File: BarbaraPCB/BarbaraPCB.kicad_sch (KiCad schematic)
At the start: 138 parts, among them J1 Conn_01x05_Pin, J2 Conn_01x05_Pin, J3 Conn_01x05_Pin_reversed, J4 Conn_01x05_Pin_reversed, SW1 SW_Push, SW10 SW_Push, SW11 SW_Push, SW12 SW_Push, SW13 SW_Push, SW14 SW_Push, SW15 SW_Push, SW16 SW_Push, SW17 SW_Push, SW18 SW_Push, SW19 SW_Push, SW2 SW_Push, SW20 SW_Push, SW21 SW_Push_1.5u, SW22 SW_Push, SW23 SW_Push, SW24 SW_Push, SW25 SW_Push, SW26 SW_Push, SW27 SW_Push, SW28 SW_Push, SW29 SW_Push_1.5u, SW3 SW_Push, SW30 SW_Push, SW31 SW_Push, SW32 SW_Push, SW33 SW_Push, SW34 SW_Push, SW35 SW_Push_1.25u, SW36 SW_Push_1.75u, SW37 SW_Push_1.75u, SW38 SW_Push_1.25u, SW39 SW_Push, SW4 SW_Push, SW40 SW_Push, SW41 SW_Push, SW42 SW_Push, SW43 SW_Push, SW44 SW_Push, SW45 SW_Push_1.5u, SW46 SW_Push_1.5u, SW47 SW_Push_1.5u, SW48 SW_Push_1.5u, SW49 SW_Push, SW5 SW_Push, SW50 SW_Push, SW51 SW_Push, SW52 SW_Push, SW53 SW_Push, SW54 SW_Push_1.25u, SW55 SW_Push_1.75u, SW56 SW_Push_1.75u, SW57 SW_Push_1.25u, SW58 SW_Push, SW59 SW_Push, SW6 SW_Push, SW60 SW_Push, SW61 SW_Push, SW62 SW_Push, SW63 SW_Push, SW64 SW_Push_1.5u, SW65 SW_Push_1.5u, SW66 SW_Push_1.5u, SW67 SW_Push_1.5u, SW7 SW_Push, SW8 SW_Push, SW9 SW_Push

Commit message: Soundbauteile hinzugefügt
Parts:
- added BZ1: Buzzer, Buzzer_Beeper:MagneticBuzzer_StarMicronics_QMB-105, symbol Device:Buzzer
- added C1: 100n, Capacitor_THT:C_Disc_D5.0mm_W2.5mm_P5.00mm, symbol Device:C
- added C2: 100n, Capacitor_SMD:C_0805_2012Metric_Pad1.18x1.45mm_HandSolder, symbol Device:C
- added D48: 1N4148, TFL:Diode-dual, symbol Diode:1N4148
- added J5: Connector for PAM8403 Amp, Connector_PinHeader_2.54mm:PinHeader_1x04_P2.54mm_Vertical, symbol Connector:Conn_01x04_Socket
- added Q2: PN2222A, Package_TO_SOT_THT:TO-92_Inline, symbol Transistor_BJT:PN2222A
- added R1, R2: 1K, TFL:Diode-dual, symbol Device:R
- added U1: RP2040-Matrix, TFL:RP2040-Gemini-BigHole, symbol PCM_marbastlib-promicroish:RP2040-Matrix
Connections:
- net row0: now also U1.4 (P29)
- new net: C1.1, C2.1, J5.4 (Pin_4), R2.2
- new net: R2.1, U1.19 (P13)
- new net: R1.1, U1.9 (P14)
- new net: BZ1.2 (-), D48.2 (A), Q2.3 (C)
- new net: Q2.2 (B), R1.2
- new net +5V: BZ1.1 (+), D48.1 (K), J5.1 (Pin_1), U1.1 (5V)
- new net GND: C1.2, C2.2, J5.2 (Pin_2), J5.3 (Pin_3), Q2.1 (E), U1.2 (GND)
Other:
- note added: "Audio GND"
- note added: "Only add one C, one is SMD, the other THT"

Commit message: Silk und diverse Kleinigkeiten. Productionready?!
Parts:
- R1, R2: footprint TFL:Diode-dual -> TFL:Resistor-dual
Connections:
- net col0: now also U1.21 (P11)
- net col1: now also U1.17 (P7)
- net col2: now also U1.16 (P6)
- net col3: now also U1.15 (P5)
- net col4: now also U1.14 (P4)
- net row0: now also U1.13 (P3); no longer U1.4 (P29)
- net row1: now also U1.22 (P10)
- net row2: now also U1.19 (P13)
- net row3: now also U1.20 (P12)
- net row4: now also U1.9 (P14)
- net row5: now also U1.8 (P15)
- net row6: now also U1.7 (P26)
- net row7: now also U1.6 (P27)
- net row8: now also U1.5 (P28)
- net row9: now also U1.4 (P29)
- net at U1.18 (P8): now also R1.1
- net at R2.1: now also U1.23 (P9); no longer U1.19 (P13)
- no-connect marks 0 -> 1
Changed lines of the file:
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@@
 		(color 0 0 0 0)
 	)
+	(no_connect
+		(at 328.93 59.69)
+	)
 	(wire
 		(pts
@@
 	(wire
 		(pts
-			(xy 311.15 82.55) (xy 311.15 88.9)
-		)
-		(stroke
-			(width 0)
-			(type default)
-		)
-	)
-	(wire
-		(pts
 			(xy 195.58 115.57) (xy 195.58 210.82)
 		)
@@
 	(wire
 		(pts
+			(xy 311.15 82.55) (xy 311.15 88.9)
+		)
+		(stroke
+			(width 0)
+			(type default)
+		)
+	)
+	(wire
+		(pts
 			(xy 154.94 252.73) (xy 128.27 252.73)
 		)
@@
 	(global_label "row8"
 		(shape input)
-		(at 384.81 40.64 90)
+		(at 328.93 64.77 0)
 		(fields_autoplaced yes)
 		(effects
@@
 		)
 		(property "Intersheetrefs" "${INTERSHEET_REFS}"
-			(at 384.81 33.1796 90)
+			(at 336.3904 64.77 0)
 			(hide yes)
 			(show_name no)
@@
 	(global_label "row1"
 		(shape input)
-		(at 267.97 40.64 90)
+		(at 313.69 82.55 270)
 		(fields_autoplaced yes)
 		(effects
@@
 				(size 1.27 1.27)
 			)
-			(justify left)
+			(justify right)
 		)
 		(property "Intersheetrefs" "${INTERSHEET_REFS}"
-			(at 267.97 33.1796 90)
+			(at 313.69 90.0104 90)
 			(hide yes)
 			(show_name no)
@@
 					(size 1.27 1.27)
 				)
-				(justify left)
+				(justify right)
 			)
 		)
@@
 	(global_label "row5"
 		(shape input)
-		(at 334.01 40.64 90)
+		(at 328.93 72.39 0)
 		(fields_autoplaced yes)
 		(effects
@@
 		)
 		(property "Intersheetrefs" "${INTERSHEET_REFS}"
-			(at 334.01 33.1796 90)
+			(at 336.3904 72.39 0)
 			(hide yes)
 			(show_name no)
@@
 	(global_label "row2"
 		(shape input)
-		(at 271.78 40.64 90)
+		(at 321.31 82.55 270)
 		(fields_autoplaced yes)
 		(effects
@@
 				(size 1.27 1.27)
 			)
-			(justify left)
+			(justify right)
 		)
 		(property "Intersheetrefs" "${INTERSHEET_REFS}"
-			(at 271.78 33.1796 90)
+			(at 321.31 90.0104 90)
 			(hide yes)
 			(show_name no)
@@
 					(size 1.27 1.27)
 				)
-				(justify left)
+				(justify right)
 			)
 		)
@@
 	(global_label "row9"
 		(shape input)
-		(at 401.32 40.64 90)
+		(at 328.93 62.23 0)
 		(fields_autoplaced yes)
 		(effects
@@
 		)
 		(property "Intersheetrefs" "${INTERSHEET_REFS}"
-			(at 401.32 33.1796 90)
+			(at 336.3904 62.23 0)
 			(hide yes)
 			(show_name no)
@@
 	(global_label "row3"
 		(shape input)
-		(at 300.99 40.64 90)
+		(at 318.77 82.55 270)
 		(fields_autoplaced yes)
 		(effects
@@
 				(size 1.27 1.27)
 			)
-			(justify left)
+			(justify right)
 		)
 		(property "Intersheetrefs" "${INTERSHEET_REFS}"
-			(at 300.99 33.1796 90)
+			(at 318.77 90.0104 90)
 			(hide yes)
 			(show_name no)
@@
 					(size 1.27 1.27)
 				)
-				(justify left)
+				(justify right)
 			)
 		)
@@
 	(global_label "col0"
 		(shape input)
-		(at 292.1 57.15 180)
+		(at 316.23 82.55 270)
 		(fields_autoplaced yes)
 		(effects
@@
 		)
 		(property "Intersheetrefs" "${INTERSHEET_REFS}"
-			(at 285.0025 57.15 0)
+			(at 316.23 89.6475 90)
 			(hide yes)
 			(show_name no)
@@
 	(global_label "col3"
 		(shape input)
-		(at 278.13 48.26 180)
+		(at 303.53 67.31 180)
 		(fields_autoplaced yes)
 		(effects
@@
 		)
 		(property "Intersheetrefs" "${INTERSHEET_REFS}"
-			(at 271.0325 48.26 0)
+			(at 296.4325 67.31 0)
 			(hide yes)
 			(show_name no)
@@
 	(global_label "col1"
 		(shape input)
-		(at 273.05 49.53 180)
+		(at 303.53 72.39 180)
 		(fields_autoplaced yes)
 		(effects
@@
 		)
 		(property "Intersheetrefs" "${INTERSHEET_REFS}"
-			(at 265.9525 49.53 0)
+			(at 296.4325 72.39 0)
 			(hide yes)
 			(show_name no)
@@
 	(global_label "col2"
 		(shape input)
-		(at 261.62 48.26 180)
+		(at 303.53 69.85 180)
 		(fields_autoplaced yes)
 		(effects
@@
 		)
 		(property "Intersheetrefs" "${INTERSHEET_REFS}"
-			(at 254.5225 48.26 0)
+			(at 296.4325 69.85 0)
 			(hide yes)
 			(show_name no)
@@
 	(global_label "row6"
 		(shape input)
-		(at 350.52 40.64 90)
+		(at 328.93 69.85 0)
 		(fields_autoplaced yes)
 		(effects
@@
 		)
 		(property "Intersheetrefs" "${INTERSHEET_REFS}"
-			(at 350.52 33.1796 90)
+			(at 336.3904 69.85 0)
 			(hide yes)
 			(show_name no)
@@
 	(global_label "col4"
 		(shape input)
-		(at 278.13 52.07 180)
+		(at 303.53 64.77 180)
 		(fields_autoplaced yes)
 		(effects
@@
 		)
 		(property "Intersheetrefs" "${INTERSHEET_REFS}"
-			(at 271.0325 52.07 0)
+			(at 296.4325 64.77 0)
 			(hide yes)
 			(show_name no)
@@
 	(global_label "row4"
 		(shape input)
-		(at 317.5 40.64 90)
+		(at 328.93 74.93 0)
 		(fields_autoplaced yes)
 		(effects
@@
 		)
 		(property "Intersheetrefs" "${INTERSHEET_REFS}"
-			(at 317.5 33.1796 90)
+			(at 336.3904 74.93 0)
 			(hide yes)
 			(show_name no)
@@
 	(global_label "row7"
 		(shape input)
-		(at 367.03 40.64 90)
+		(at 328.93 67.31 0)
 		(fields_autoplaced yes)
 		(effects
@@
 		)
 		(property "Intersheetrefs" "${INTERSHEET_REFS}"
-			(at 367.03 33.1796 90)
+			(at 336.3904 67.31 0)
 			(hide yes)
 			(show_name no)
@@
 		(lib_id "PCM_marbastlib-promicroish:RP2040-Matrix")
 		(at 316.23 68.58 0)
+		(mirror y)
 		(unit 1)
 		(body_style 1)
@@
 		)
 		(property "Datasheet" "https://www.waveshare.com/rp2040-matrix.htm"
-			(at 303.53 54.61 0)
+			(at 328.93 54.61 0)
 			(hide yes)
 			(show_name no)
@@
 			)
 		)
-		(property "Footprint" "TFL:Diode-dual"
+		(property "Footprint" "TFL:Resistor-dual"
 			(at 299.72 73.152 90)
 			(hide yes)
@@
 	(symbol
 		(lib_id "power:+5V")
-		(at 303.53 54.61 90)
+		(at 328.93 54.61 270)
 		(unit 1)
 		(body_style 1)
@@
 		(fields_autoplaced yes)
 		(property "Reference" "#PWR02"
-			(at 307.34 54.61 0)
+			(at 325.12 54.61 0)
 			(hide yes)
 			(show_name no)
@@
 		)
 		(property "Value" "+5V"
-			(at 299.72 54.6099 90)
+			(at 332.74 54.6099 90)
 			(show_name no)
 			(do_not_autoplace no)
@@
 		)
 		(property "Footprint" ""
-			(at 303.53 54.61 0)
+			(at 328.93 54.61 0)
 			(hide yes)
 			(show_name no)
@@
 		)
 		(property "Datasheet" ""
-			(at 303.53 54.61 0)
+			(at 328.93 54.61 0)
 			(hide yes)
 			(show_name no)
@@
 		)
 		(property "Description" "Power symbol creates a global label with name \"+5V\""
-			(at 303.53 54.61 0)
+			(at 328.93 54.61 0)
 			(hide yes)
 			(show_name no)
@@
 			)
 		)
-		(property "Footprint" "TFL:Diode-dual"
+		(property "Footprint" "TFL:Resistor-dual"
 			(at 309.372 92.71 90)
 			(hide yes)
@@
 	(symbol
 		(lib_id "power:GND")
-		(at 303.53 57.15 270)
+		(at 328.93 57.15 90)
 		(unit 1)
 		(body_style 1)
@@
 		(fields_autoplaced yes)
 		(property "Reference" "#PWR01"
-			(at 297.18 57.15 0)
+			(at 335.28 57.15 0)
 			(hide yes)
 			(show_name no)
@@
 		)
 		(property "Value" "GND"
-			(at 299.72 57.1499 90)
+			(at 332.74 57.1499 90)
 			(show_name no)
 			(do_not_autoplace no)
@@
 		)
 		(property "Footprint" ""
-			(at 303.53 57.15 0)
+			(at 328.93 57.15 0)
 			(hide yes)
 			(show_name no)
@@
 		)
 		(property "Datasheet" ""
-			(at 303.53 57.15 0)
+			(at 328.93 57.15 0)
 			(hide yes)
 			(show_name no)
@@
 		)
 		(property "Description" "Power symbol creates a global label with name \"GND\" , ground"
-			(at 303.53 57.15 0)
+			(at 328.93 57.15 0)
 			(hide yes)
 			(show_name no)

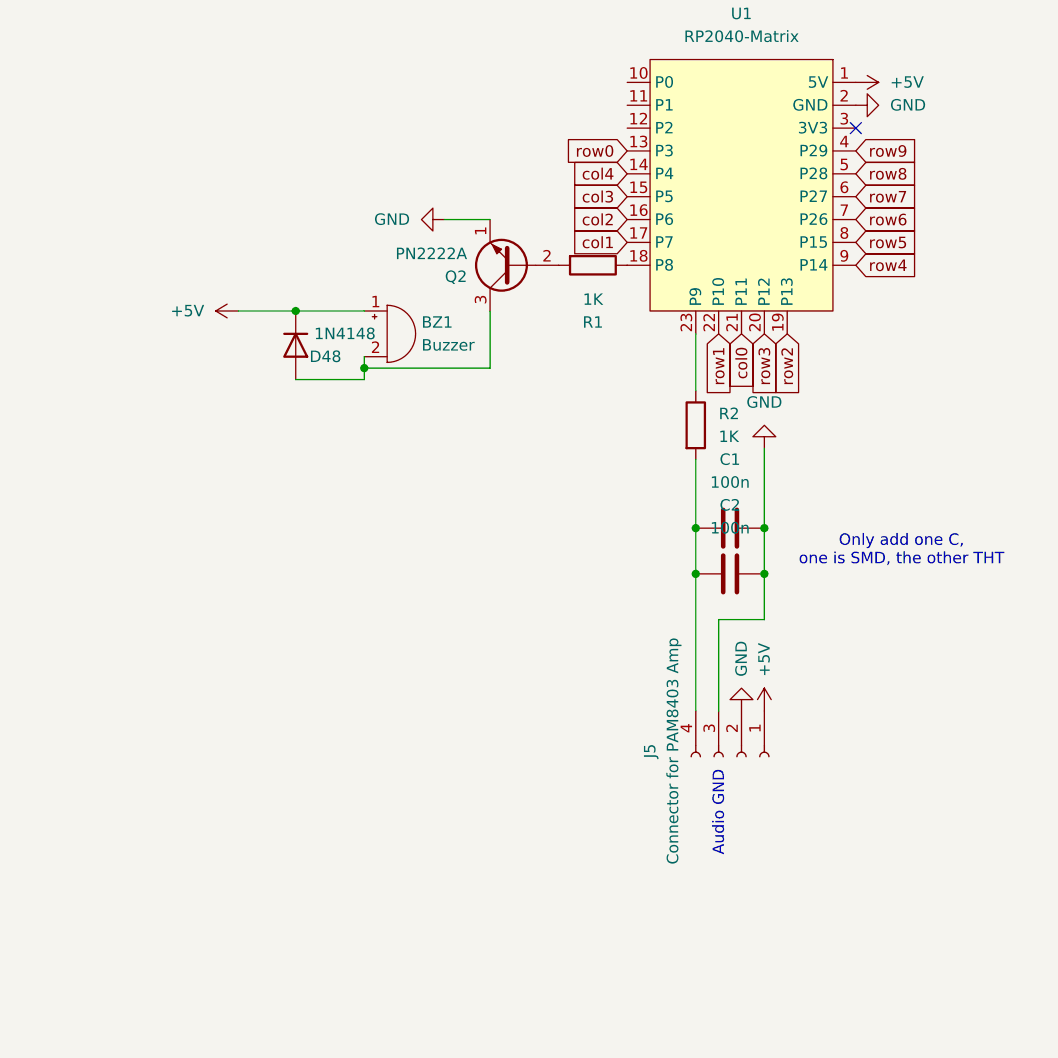
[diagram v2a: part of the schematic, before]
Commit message: Simplified audio-part. Not amp or transistor needed.
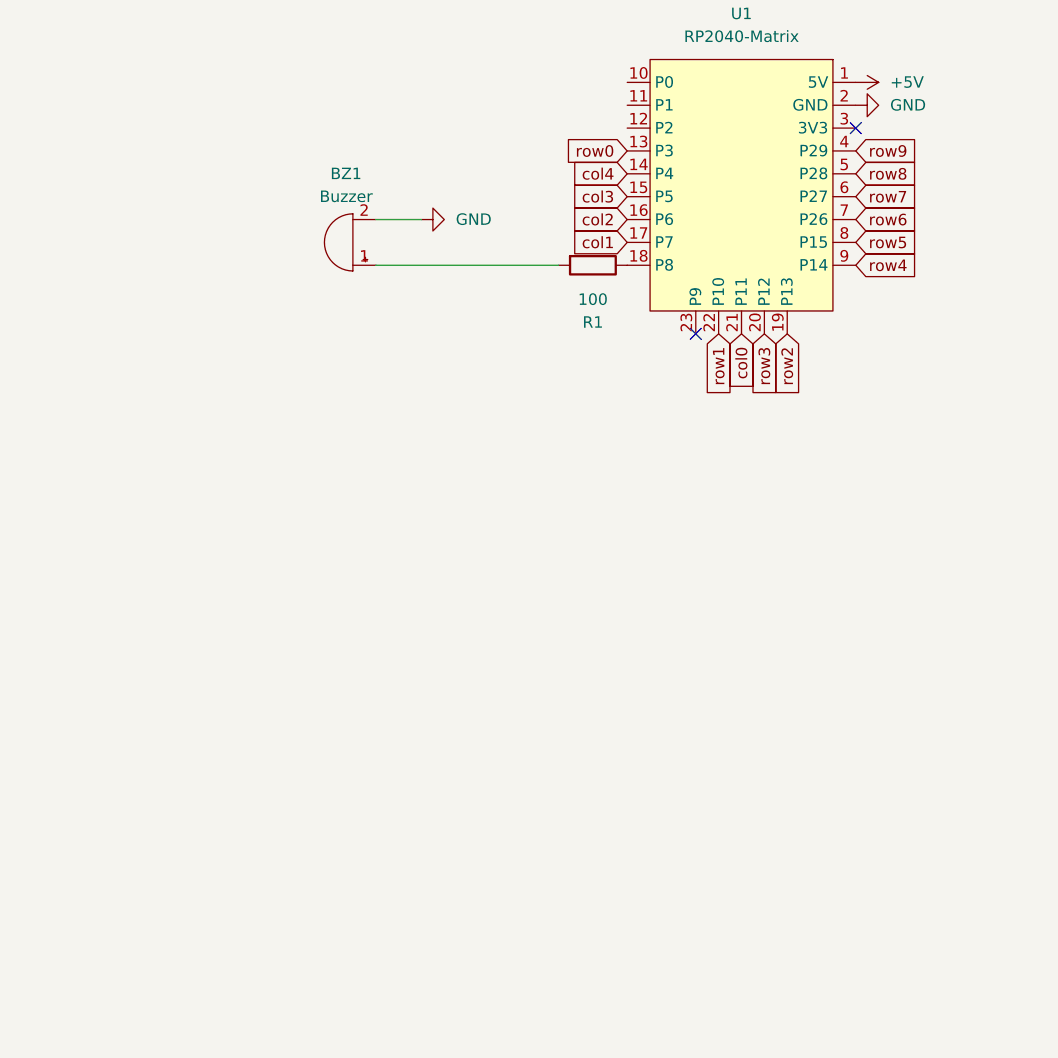
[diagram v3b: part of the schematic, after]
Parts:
- removed C1: 100n, Capacitor_THT:C_Disc_D5.0mm_W2.5mm_P5.00mm, symbol Device:C
- removed C2: 100n, Capacitor_SMD:C_0805_2012Metric_Pad1.18x1.45mm_HandSolder, symbol Device:C
- removed D48: 1N4148, TFL:Diode-dual, symbol Diode:1N4148
- removed J5: Connector for PAM8403 Amp, Connector_PinHeader_2.54mm:PinHeader_1x04_P2.54mm_Vertical, symbol Connector:Conn_01x04_Socket
- removed Q2: PN2222A, Package_TO_SOT_THT:TO-92_Inline, symbol Transistor_BJT:PN2222A
- removed R2: 1K, TFL:Resistor-dual, symbol Device:R
- R1: value 1K -> 100
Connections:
- net +5V: no longer BZ1.1 (+)
- net GND: now also BZ1.2 (-)
- net at R1.2: now also BZ1.1 (+)
- no-connect marks 1 -> 2
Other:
- note removed: "Audio GND"
- note removed: "Only add one C, one is SMD, the other THT"
- moved on the sheet: BZ1
